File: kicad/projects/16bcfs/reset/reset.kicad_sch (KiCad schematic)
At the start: 26 parts, among them J1 Conn_01x16_Pin, U1 74HC00, U2 74HC08, U3 74HC32, U4 74HC00, U5 74HC74, U6 74HC00, U7 74HC02, U8 74HC123, U9 74HC03

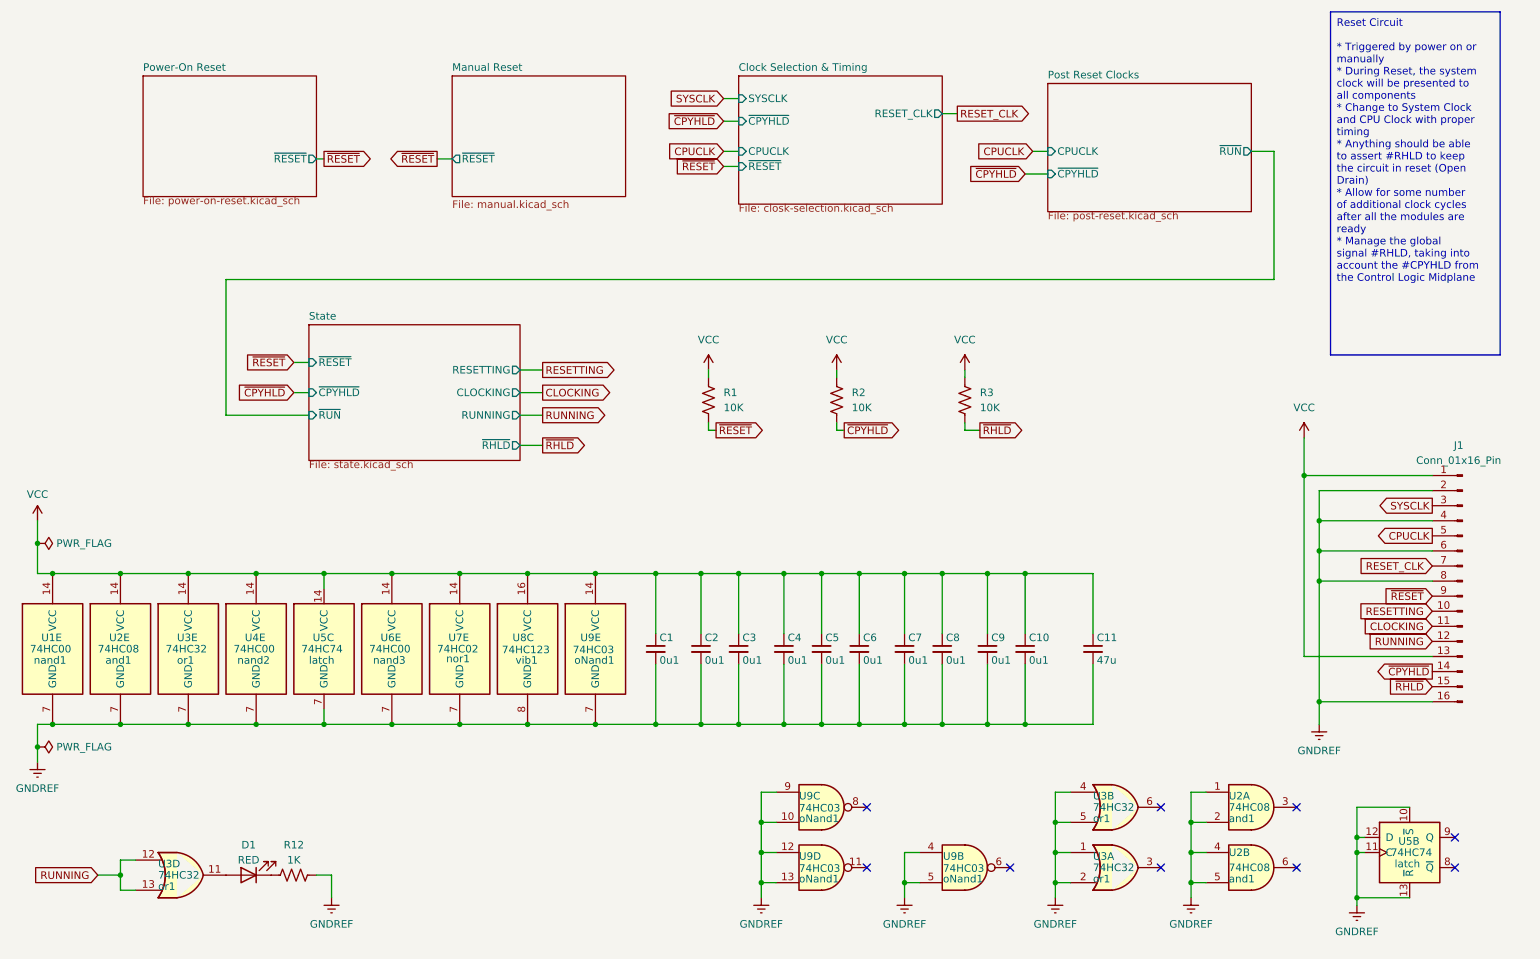
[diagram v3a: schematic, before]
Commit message: Address some issues with the Reset Logic
There were a couple of fixes.  One in relation to how the 74xx123 IC was
emulated and others to the schematic to address issues in real life in
the breadboard prototype.
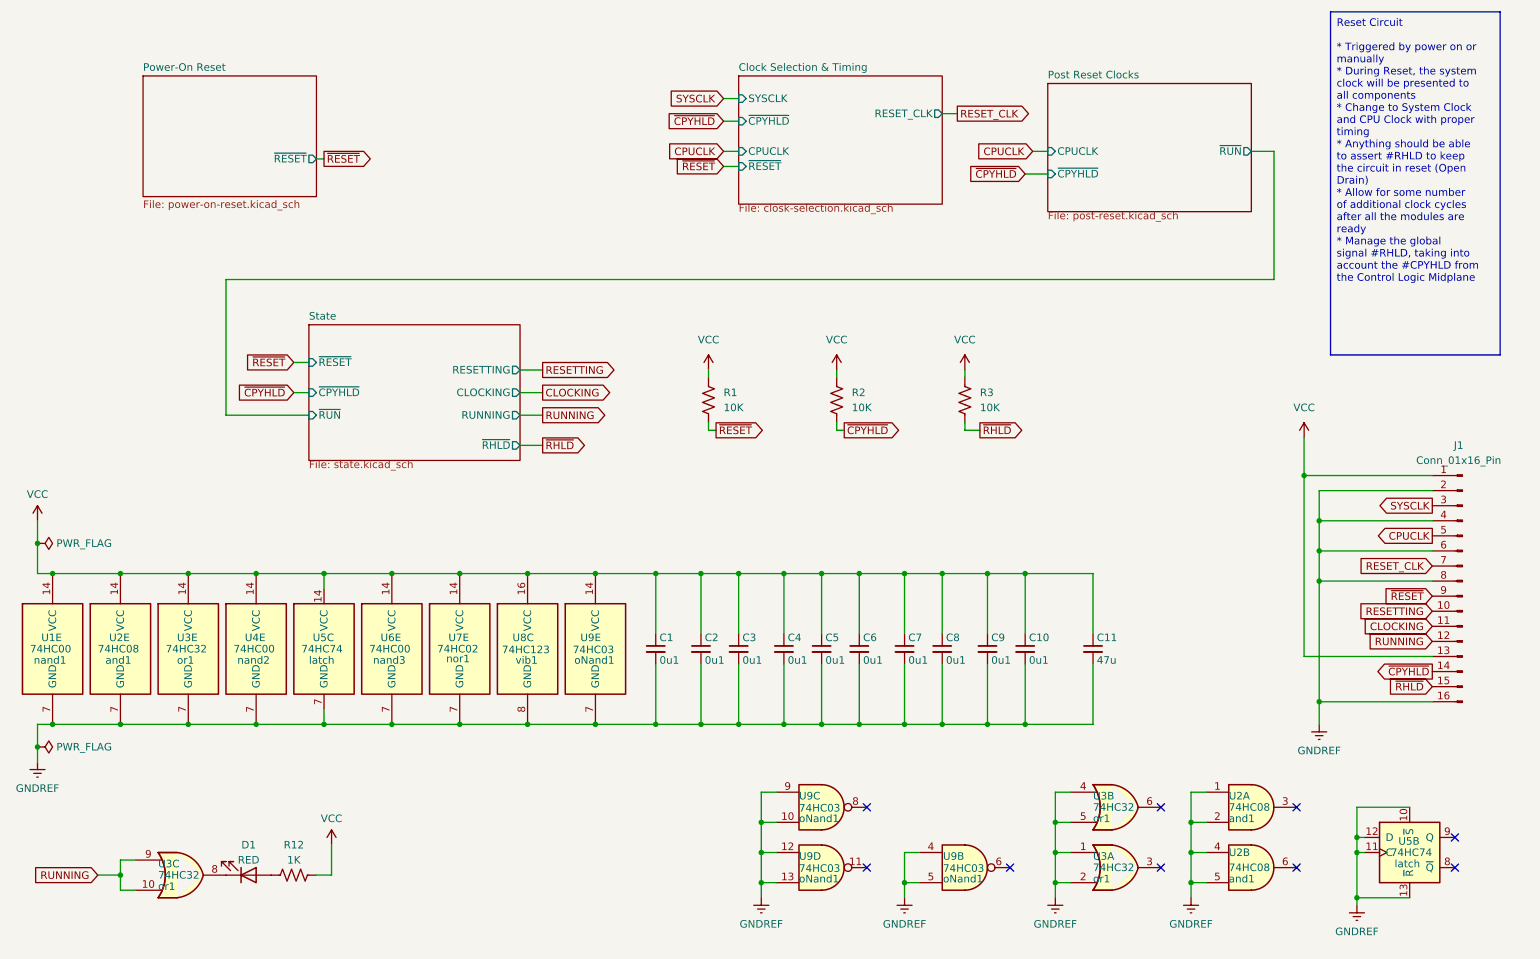
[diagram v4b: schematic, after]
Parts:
- removed unit 4 of U3
- added unit 3 of U3
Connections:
- net GNDREF: no longer R12.2
- net RUNNING: now also U3.10, U3.9
- net VCC: now also R12.2
- net at D1.1 (K): now also U3.8; no longer R12.1
- net at D1.2 (A): now also R12.1
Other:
- removed sheet Manual Reset
- moved on the sheet: D1
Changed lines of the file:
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@@
+    (stroke (width 0) (type default))
+  )
+  (wire (pts (xy 67.31 156.21) (xy 67.31 161.29))
     (stroke (width 0) (type default))
   )
@@
     (stroke (width 0) (type default))
   )
+  (wire (pts (xy 240.03 149.86) (xy 240.03 154.94))
+    (stroke (width 0) (type default))
+  )
+  (wire (pts (xy 231.14 93.98) (xy 231.14 124.46))
+    (stroke (width 0) (type default))
+  )
+  (wire (pts (xy 191.77 152.4) (xy 189.23 152.4))
+    (stroke (width 0) (type default))
+  )
+  (wire (pts (xy 212.09 162.56) (xy 212.09 165.1))
+    (stroke (width 0) (type default))
+  )
+  (wire (pts (xy 111.76 110.49) (xy 121.92 110.49))
+    (stroke (width 0) (type default))
+  )
+  (wire (pts (xy 233.68 111.76) (xy 233.68 132.08))
+    (stroke (width 0) (type default))
+  )
+  (wire (pts (xy 233.68 132.08) (xy 233.68 135.89))
+    (stroke (width 0) (type default))
+  )
+  (wire (pts (xy 66.04 110.49) (xy 66.04 113.03))
+    (stroke (width 0) (type default))
+  )
+  (wire (pts (xy 143.51 120.65) (xy 143.51 110.49))
+    (stroke (width 0) (type default))
+  )
+  (wire (pts (xy 129.54 125.73) (xy 129.54 135.89))
+    (stroke (width 0) (type default))
+  )
+  (wire (pts (xy 177.8 135.89) (xy 184.15 135.89))
+    (stroke (width 0) (type default))
+  )
   (wire (pts (xy 64.77 161.29) (xy 67.31 161.29))
     (stroke (width 0) (type default))
   )
-  (wire (pts (xy 240.03 149.86) (xy 240.03 154.94))
-    (stroke (width 0) (type default))
-  )
-  (wire (pts (xy 231.14 93.98) (xy 231.14 124.46))
-    (stroke (width 0) (type default))
-  )
-  (wire (pts (xy 191.77 152.4) (xy 189.23 152.4))
-    (stroke (width 0) (type default))
-  )
-  (wire (pts (xy 212.09 162.56) (xy 212.09 165.1))
-    (stroke (width 0) (type default))
-  )
-  (wire (pts (xy 111.76 110.49) (xy 121.92 110.49))
-    (stroke (width 0) (type default))
-  )
-  (wire (pts (xy 233.68 111.76) (xy 233.68 132.08))
-    (stroke (width 0) (type default))
-  )
-  (wire (pts (xy 233.68 132.08) (xy 233.68 135.89))
-    (stroke (width 0) (type default))
-  )
-  (wire (pts (xy 66.04 110.49) (xy 66.04 113.03))
-    (stroke (width 0) (type default))
-  )
-  (wire (pts (xy 143.51 120.65) (xy 143.51 110.49))
-    (stroke (width 0) (type default))
-  )
-  (wire (pts (xy 129.54 125.73) (xy 129.54 135.89))
-    (stroke (width 0) (type default))
-  )
-  (wire (pts (xy 177.8 135.89) (xy 184.15 135.89))
-    (stroke (width 0) (type default))
-  )
   (wire (pts (xy 184.15 120.65) (xy 184.15 110.49))
     (stroke (width 0) (type default))
@@
     (stroke (width 0) (type default))
   )
-  (wire (pts (xy 85.09 40.64) (xy 87.63 40.64))
-    (stroke (width 0) (type default))
-  )
   (wire (pts (xy 231.14 87.63) (xy 231.14 93.98))
     (stroke (width 0) (type default))
@@
   )
   (wire (pts (xy 133.35 34.29) (xy 135.89 34.29))
-    (stroke (width 0) (type default))
-  )
-  (wire (pts (xy 67.31 161.29) (xy 67.31 165.1))
     (stroke (width 0) (type default))
   )
@@
     (effects (font (size 1.27 1.27)) (justify right))
     (property "Intersheetrefs" "${INTERSHEET_REFS}" (at 174.9962 39.37 0)
-      (effects (font (size 1.27 1.27)) (justify right) hide)
-    )
-  )
-  (global_label "~{RESET}" (shape output) (at 85.09 40.64 180) (fields_autoplaced)
-    (effects (font (size 1.27 1.27)) (justify right))
-    (property "Intersheetrefs" "${INTERSHEET_REFS}" (at 76.3597 40.64 0)
       (effects (font (size 1.27 1.27)) (justify right) hide)
     )
@@
         (path "/d0ae44e5-d74e-4df6-bf3d-e0535c5a7785"
           (reference "C4") (unit 1)
+        )
+      )
+    )
+  )
+  (symbol (lib_id "eryjus:74HC32") (at 41.91 161.29 0) (unit 3)
+    (in_bom yes) (on_board yes) (dnp no)
+    (property "Reference" "U3" (at 38.1 159.385 0)
+      (effects (font (size 1.27 1.27)) (justify left))
+    )
+    (property "Value" "74HC32" (at 38.1 161.29 0)
+      (effects (font (size 1.27 1.27)) (justify left))
+    )
+    (property "Footprint" "" (at 41.91 161.29 0)
+      (effects (font (size 1.27 1.27)) hide)
+    )
+    (property "Datasheet" "http://www.ti.com/lit/gpn/sn74HC32" (at 41.91 161.29 0)
+      (effects (font (size 1.27 1.27)) hide)
+    )
+    (property "name" "or1" (at 38.1 163.195 0)
+      (effects (font (size 1.27 1.27)) (justify left))
+    )
+    (pin "5")
+    (pin "4")
+    (pin "12")
+    (pin "1")
+    (pin "11")
+    (pin "6")
+    (pin "3")
+    (pin "14")
+    (pin "13")
+    (pin "7")
+    (pin "10")
+    (pin "2")
+    (pin "8")
+    (pin "9")
+    (instances
+      (project "reset"
+        (path "/d0ae44e5-d74e-4df6-bf3d-e0535c5a7785"
+          (reference "U3") (unit 3)
         )
       )
@@
     )
   )
-  (symbol (lib_id "power:GNDREF") (at 67.31 165.1 0) (unit 1)
-    (in_bom yes) (on_board yes) (dnp no) (fields_autoplaced)
-    (property "Reference" "#PWR025" (at 67.31 171.45 0)
-      (effects (font (size 1.27 1.27)) hide)
-    )
-    (property "Value" "GNDREF" (at 67.31 169.545 0)
-      (effects (font (size 1.27 1.27)))
-    )
-    (property "Footprint" "" (at 67.31 165.1 0)
-      (effects (font (size 1.27 1.27)) hide)
-    )
-    (property "Datasheet" "" (at 67.31 165.1 0)
-      (effects (font (size 1.27 1.27)) hide)
-    )
-    (pin "1")
-    (instances
-      (project "reset"
-        (path "/d0ae44e5-d74e-4df6-bf3d-e0535c5a7785"
-          (reference "#PWR025") (unit 1)
-        )
-      )
-    )
-  )
   (symbol (lib_id "eryjus:74HC03") (at 149.86 149.86 0) (unit 3)
     (in_bom yes) (on_board yes) (dnp no)
@@
     )
   )
-  (symbol (lib_id "Device:LED") (at 53.34 161.29 180) (unit 1)
+  (symbol (lib_id "Device:LED") (at 53.34 161.29 0) (mirror x) (unit 1)
     (in_bom yes) (on_board yes) (dnp no)
     (property "Reference" "D1" (at 53.34 156.21 0)
@@
     )
   )
+  (symbol (lib_id "power:VCC") (at 67.31 156.21 0) (mirror y) (unit 1)
+    (in_bom yes) (on_board yes) (dnp no)
+    (property "Reference" "#PWR08" (at 67.31 160.02 0)
+      (effects (font (size 1.27 1.27)) hide)
+    )
+    (property "Value" "VCC" (at 67.31 151.765 0)
+      (effects (font (size 1.27 1.27)))
+    )
+    (property "Footprint" "" (at 67.31 156.21 0)
+      (effects (font (size 1.27 1.27)) hide)
+    )
+    (property "Datasheet" "" (at 67.31 156.21 0)
+      (effects (font (size 1.27 1.27)) hide)
+    )
+    (pin "1")
+    (instances
+      (project "reset"
+        (path "/d0ae44e5-d74e-4df6-bf3d-e0535c5a7785"
+          (reference "#PWR08") (unit 1)
+        )
+      )
+    )
+  )
   (symbol (lib_id "Device:C_Small") (at 121.92 123.19 0) (unit 1)
     (in_bom yes) (on_board yes) (dnp no)
@@
         (path "/d0ae44e5-d74e-4df6-bf3d-e0535c5a7785"
           (reference "#PWR01") (unit 1)
-        )
-      )
-    )
-  )
-  (symbol (lib_id "eryjus:74HC32") (at 41.91 161.29 0) (unit 4)
-    (in_bom yes) (on_board yes) (dnp no)
-    (property "Reference" "U3" (at 38.1 159.385 0)
-      (effects (font (size 1.27 1.27)) (justify left))
-    )
-    (property "Value" "74HC32" (at 38.1 161.29 0)
-      (effects (font (size 1.27 1.27)) (justify left))
-    )
-    (property "Footprint" "" (at 41.91 161.29 0)
-      (effects (font (size 1.27 1.27)) hide)
-    )
-    (property "Datasheet" "http://www.ti.com/lit/gpn/sn74HC32" (at 41.91 161.29 0)
-      (effects (font (size 1.27 1.27)) hide)
-    )
-    (property "name" "or1" (at 38.1 163.195 0)
-      (effects (font (size 1.27 1.27)) (justify left))
-    )
-    (pin "5")
-    (pin "4")
-    (pin "12")
-    (pin "1")
-    (pin "11")
-    (pin "6")
-    (pin "3")
-    (pin "14")
-    (pin "13")
-    (pin "7")
-    (pin "10")
-    (pin "2")
-    (pin "8")
-    (pin "9")
-    (instances
-      (project "reset"
-        (path "/d0ae44e5-d74e-4df6-bf3d-e0535c5a7785"
-          (reference "U3") (unit 4)
         )
       )
@@
     )
   )
-  (sheet (at 87.63 26.67) (size 29.21 20.32) (fields_autoplaced)
-    (stroke (width 0.1524) (type solid))
-    (fill (color 0 0 0 0.0000))
-    (property "Sheetname" "Manual Reset" (at 87.63 25.9584 0)
-      (effects (font (size 1.27 1.27)) (justify left bottom))
-    )
-    (property "Sheetfile" "manual.kicad_sch" (at 87.63 47.5746 0)
-      (effects (font (size 1.27 1.27)) (justify left top))
-    )
-    (pin "~{RESET}" output (at 87.63 40.64 180)
-      (effects (font (size 1.27 1.27)) (justify left))
-    )
-    (instances
-      (project "reset"
-        (path "/d0ae44e5-d74e-4df6-bf3d-e0535c5a7785" (page "3"))
-      )
-    )
-  )
   (sheet (at 35.56 26.67) (size 29.21 20.32) (fields_autoplaced)
     (stroke (width 0.1524) (type solid))
@@
       (effects (font (size 1.27 1.27)) (justify left bottom))
     )
-    (property "Sheetfile" "power-on-reset.kicad_sch" (at 35.56 46.9396 0)
+    (property "Sheetfile" "power-on-reset.kicad_sch" (at 35.56 47.5746 0)
       (effects (font (size 1.27 1.27)) (justify left top))
     )

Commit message: Rename RESET_CLK
This also forces a rename of the SYSCLK on the Reset Schematic to be
HS_CLK.  The new name of the RESET_CLK is SYS_CLK.
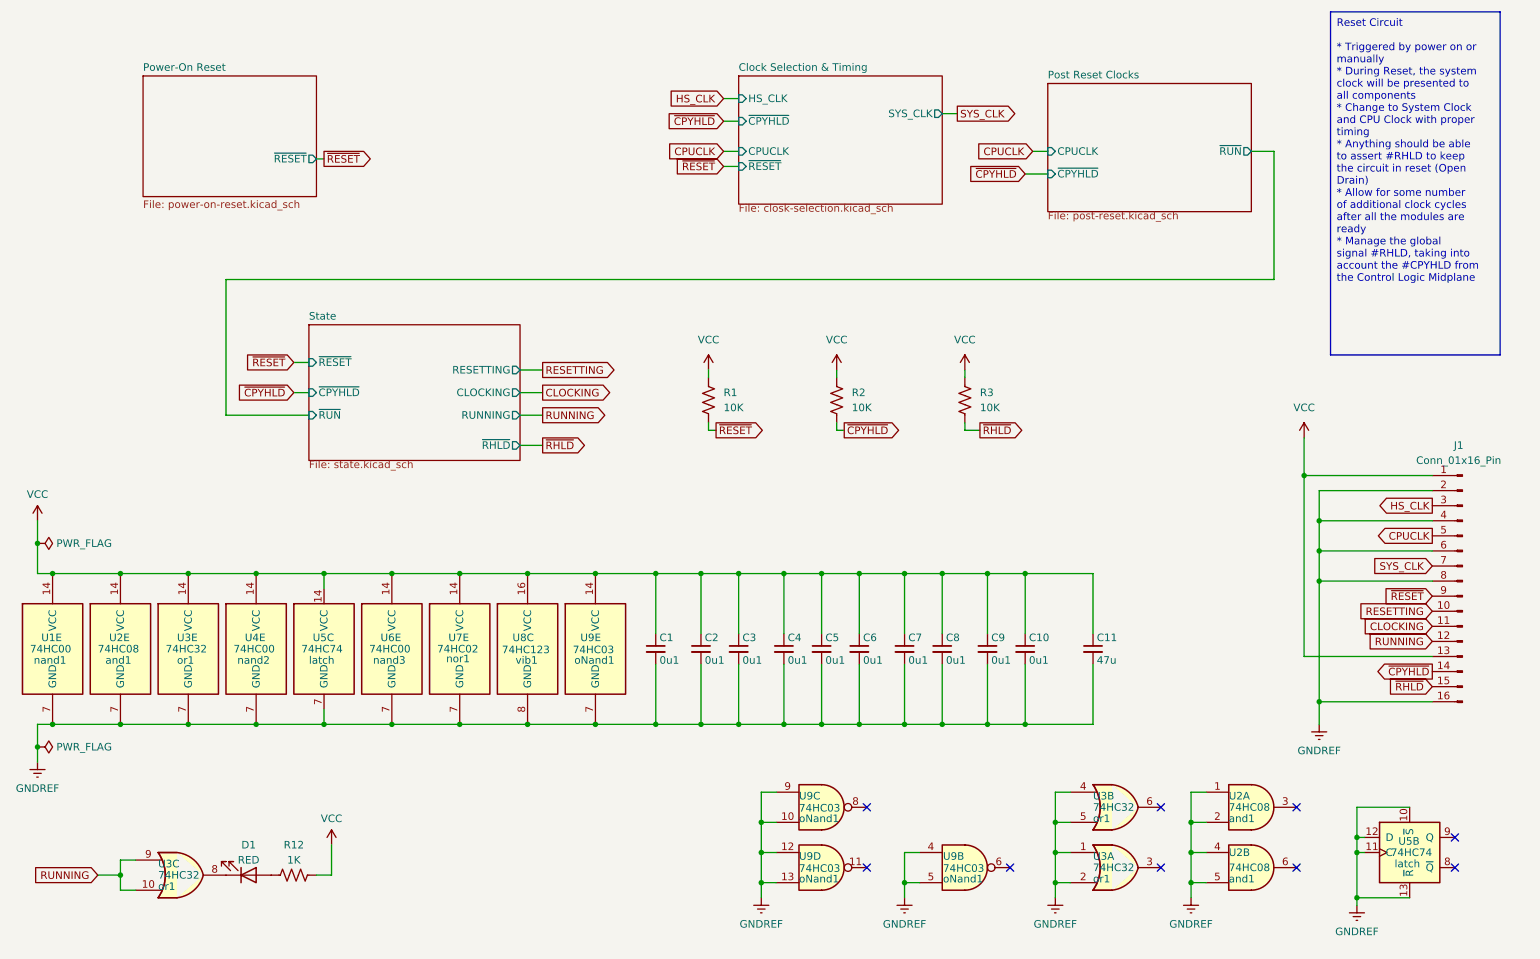
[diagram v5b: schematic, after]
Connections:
- net RESET_CLK renamed SYS_CLK
- net SYSCLK renamed HS_CLK
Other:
- sheet Clock Selection & Timing ports: added HS_CLK, SYS_CLK; removed RESET_CLK, SYSCLK
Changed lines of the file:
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@@
     )
   )
-  (global_label "RESET_CLK" (shape output) (at 172.72 33.02 0) (fields_autoplaced)
+  (global_label "SYS_CLK" (shape output) (at 172.72 33.02 0) (fields_autoplaced)
     (effects (font (size 1.27 1.27)) (justify left))
-    (property "Intersheetrefs" "${INTERSHEET_REFS}" (at 185.986 33.02 0)
+    (property "Intersheetrefs" "${INTERSHEET_REFS}" (at 183.7485 33.02 0)
       (effects (font (size 1.27 1.27)) (justify left) hide)
     )
@@
     )
   )
-  (global_label "SYSCLK" (shape input) (at 133.35 30.48 180) (fields_autoplaced)
+  (global_label "HS_CLK" (shape input) (at 133.35 30.48 180) (fields_autoplaced)
     (effects (font (size 1.27 1.27)) (justify right))
     (property "Intersheetrefs" "${INTERSHEET_REFS}" (at 123.2891 30.48 0)
@@
     )
   )
-  (global_label "RESET_CLK" (shape input) (at 252.73 109.22 180) (fields_autoplaced)
+  (global_label "SYS_CLK" (shape input) (at 252.73 109.22 180) (fields_autoplaced)
     (effects (font (size 1.27 1.27)) (justify right))
-    (property "Intersheetrefs" "${INTERSHEET_REFS}" (at 239.464 109.22 0)
+    (property "Intersheetrefs" "${INTERSHEET_REFS}" (at 241.7015 109.22 0)
       (effects (font (size 1.27 1.27)) (justify right) hide)
     )
@@
     )
   )
-  (global_label "SYSCLK" (shape output) (at 252.73 99.06 180) (fields_autoplaced)
+  (global_label "HS_CLK" (shape output) (at 252.73 99.06 180) (fields_autoplaced)
     (effects (font (size 1.27 1.27)) (justify right))
     (property "Intersheetrefs" "${INTERSHEET_REFS}" (at 242.6691 99.06 0)
@@
       (effects (font (size 1.27 1.27)) (justify left))
     )
-    (pin "SYSCLK" input (at 135.89 30.48 180)
+    (pin "HS_CLK" input (at 135.89 30.48 180)
       (effects (font (size 1.27 1.27)) (justify left))
     )
@@
       (effects (font (size 1.27 1.27)) (justify left))
     )
-    (pin "RESET_CLK" output (at 170.18 33.02 0)
+    (pin "SYS_CLK" output (at 170.18 33.02 0)
       (effects (font (size 1.27 1.27)) (justify right))
     )
